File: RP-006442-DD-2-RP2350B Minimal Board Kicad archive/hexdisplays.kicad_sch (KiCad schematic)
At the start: 0 parts

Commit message: Created HT16K33-28SOP symbol
assigned new symbol footprint the pre-defined footprint for SOP-28 package
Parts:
- added U8: HT16K33A-28SOP, Package_SO:SOP-28_8.4x18.16mm_P1.27mm, symbol Driver_LED:HT16K33A-28SOP
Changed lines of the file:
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@@
 	(generator_version "9.0")
 	(paper "A4")
+	(symbol
+		(lib_id "Driver_LED:HT16K33A-28SOP")
+		(at 113.03 82.55 0)
+		(unit 1)
+		(exclude_from_sim no)
+		(in_bom yes)
+		(on_board yes)
+		(dnp no)
+		(fields_autoplaced yes)
+		(property "Reference" "U8"
+			(at 128.905 76.2 0)
+			(effects
+				(font
+					(size 1.27 1.27)
+				)
+			)
+		)
+		(property "Value" "HT16K33A-28SOP"
+			(at 128.905 78.74 0)
+			(effects
+				(font
+					(size 1.27 1.27)
+				)
+			)
+		)
+		(property "Footprint" "Package_SO:SOP-28_8.4x18.16mm_P1.27mm"
+			(at 129.032 121.412 0)
+			(effects
+				(font
+					(size 1.27 1.27)
+				)
+				(hide yes)
+			)
+		)
+		(property "Datasheet" "https://www.holtek.com/webapi/116711/HT16K33Av102.pdf"
+			(at 127.254 78.232 0)
+			(effects
+				(font
+					(size 1.27 1.27)
+				)
+				(hide yes)
+			)
+		)
+		(property "Description" "RAM Mapping 16×8 LED Controller Driver with Keyscan"
+			(at 127.254 75.946 0)
+			(effects
+				(font
+					(size 1.27 1.27)
+				)
+				(hide yes)
+			)
+		)
+		(pin "1"
+		)
+		(pin "7"
+		)
+		(pin "6"
+		)
+		(pin "5"
+		)
+		(pin "4"
+		)
+		(pin "8"
+		)
+		(pin "9"
+		)
+		(pin "19"
+		)
+		(pin "15"
+		)
+		(pin "20"
+		)
+		(pin "2"
+		)
+		(pin "23"
+		)
+		(pin "24"
+		)
+		(pin "25"
+		)
+		(pin "26"
+		)
+		(pin "28"
+		)
+		(pin "27"
+		)
+		(pin "14"
+		)
+		(pin "13"
+		)
+		(pin "12"
+		)
+		(pin "11"
+		)
+		(pin "10"
+		)
+		(pin "22"
+		)
+		(pin "21"
+		)
+		(pin "3"
+		)
+		(pin "16"
+		)
+		(pin "18"
+		)
+		(pin "17"
+		)
+		(instances
+			(project ""
+				(path "/94683f5c-9cd9-448e-be96-9792537b5cb8/09473c75-4602-45fc-a2db-44d591bf96bf"
+					(reference "U8")
+					(unit 1)
+				)
+			)
+		)
+	)
 )

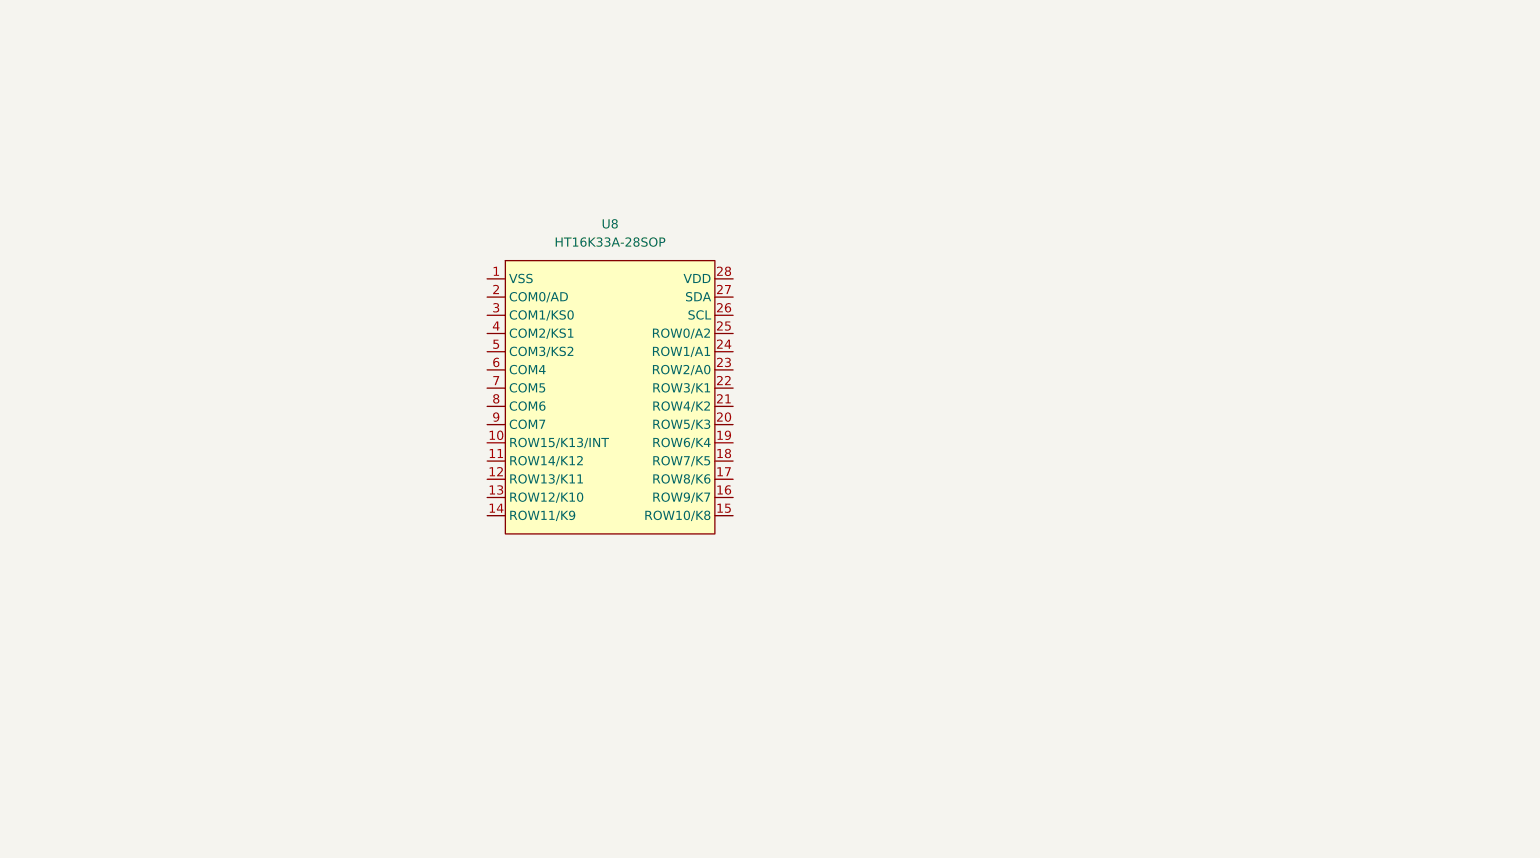
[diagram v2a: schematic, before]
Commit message: Update hex displays
Added 7-segment display symbol, labels, i2c pull-up resistors, capacitor.

Synced added components to pcb.
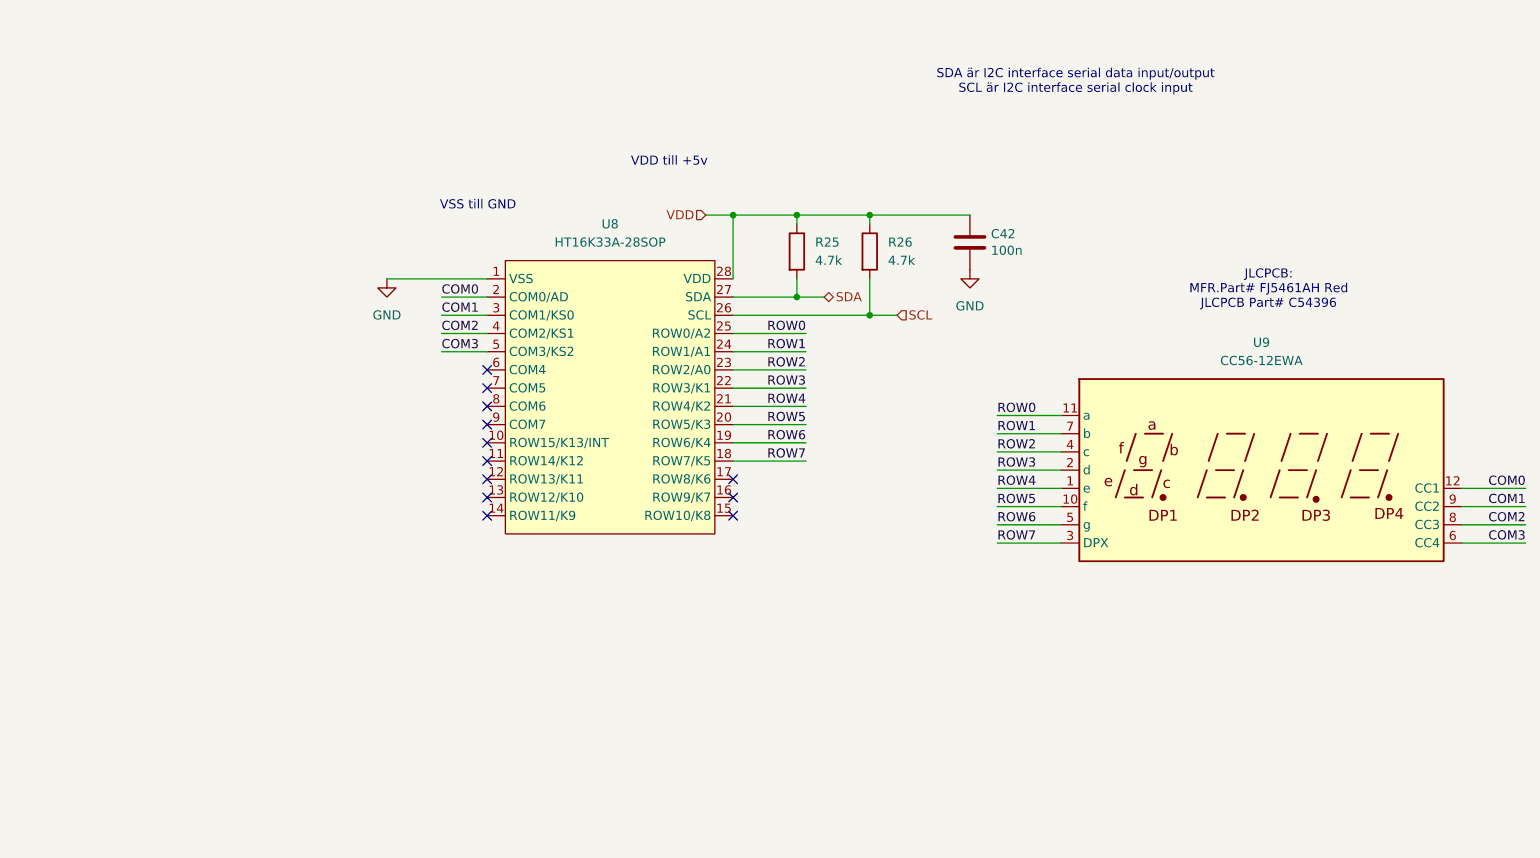
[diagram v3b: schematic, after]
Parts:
- added C42: 100n, Capacitor_SMD:C_0402_1005Metric, symbol Device:C
- added R25, R26: 4.7k, Resistor_SMD:R_0402_1005Metric, symbol Device:R
- added U9: CC56-12EWA, Display_7Segment:CA56-12EWA, symbol Display_Character:CC56-12EWA
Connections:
- net GND: now reaches U8.1 (VSS)
- net GND: now also C42.2
- net ROW7: now reaches U8.18 (ROW7/K5)
- net ROW7: now also U9.3 (DPX)
- net ROW6: now reaches U8.19 (ROW6/K4)
- net ROW6: now also U9.5 (g)
- net COM0: now reaches U8.2 (COM0/AD)
- net COM0: now also U9.12 (CC1)
- net ROW5: now reaches U8.20 (ROW5/K3)
- net ROW5: now also U9.10 (f)
- net ROW4: now reaches U8.21 (ROW4/K2)
- net ROW4: now also U9.1 (e)
- net ROW3: now reaches U8.22 (ROW3/K1)
- net ROW3: now also U9.2 (d)
- net ROW2: now reaches U8.23 (ROW2/A0)
- net ROW2: now also U9.4 (c)
- net ROW1: now reaches U8.24 (ROW1/A1)
- net ROW1: now also U9.7 (b)
- net ROW0: now reaches U8.25 (ROW0/A2)
- net ROW0: now also U9.11 (a)
- net SCL: now reaches U8.26 (SCL)
- net SCL: now also R26.2
- net SDA: now reaches U8.27 (SDA)
- net SDA: now also R25.2
- net VDD: now reaches U8.28 (VDD)
- net VDD: now also C42.1, R25.1, R26.1
- net COM1: now reaches U8.3 (COM1/KS0)
- net COM1: now also U9.9 (CC2)
- net COM2: now reaches U8.4 (COM2/KS1)
- net COM2: now also U9.8 (CC3)
- net COM3: now reaches U8.5 (COM3/KS2)
- net COM3: now also U9.6 (CC4)
- no-connect marks 0 -> 12
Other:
- note added: "JLCPCB: MFR.Part# FJ5461AH Red JLCPCB Part# C54396"
- note added: "SDA är I2C interface serial data input/output SCL är I2C interface serial clock input"
- note added: "VDD till +5v"
- note added: "VSS till GND"

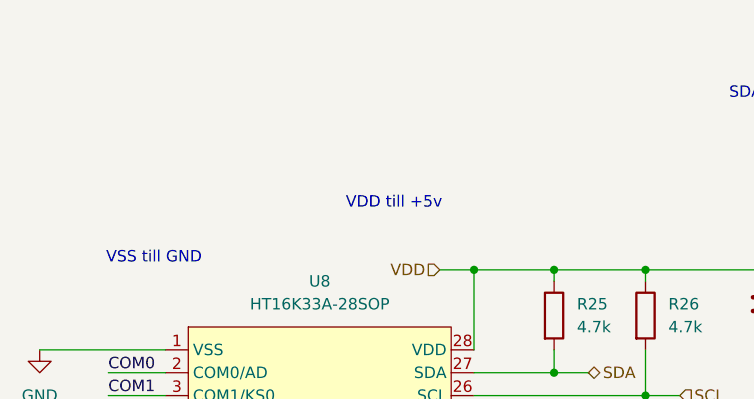
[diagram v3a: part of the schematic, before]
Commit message: Update hexdisplays.kicad_sch
added NCP1117-5.0 linear voltage regulator symbol
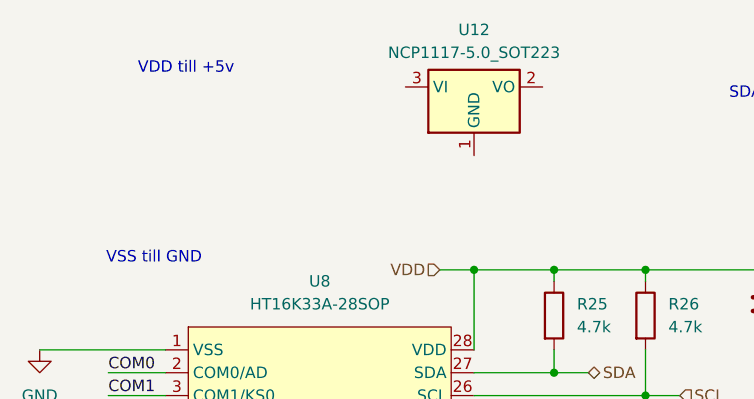
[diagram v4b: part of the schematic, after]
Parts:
- added U12: NCP1117-5.0_SOT223, Package_TO_SOT_SMD:SOT-223-3_TabPin2, symbol Regulator_Linear:NCP1117-5.0_SOT223
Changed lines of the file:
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@@
 	(text "VDD till +5v"
 		(exclude_from_sim no)
-		(at 137.16 67.564 0)
+		(at 114.046 52.578 0)
 		(effects
 			(font
@@
 					(unit 1)
 				)
+			)
+		)
+	)
+	(symbol
+		(lib_id "Regulator_Linear:NCP1117-5.0_SOT223")
+		(at 146.05 54.61 0)
+		(unit 1)
+		(exclude_from_sim no)
+		(in_bom yes)
+		(on_board yes)
+		(dnp no)
+		(fields_autoplaced yes)
+		(property "Reference" "U12"
+			(at 146.05 48.26 0)
+			(effects
+				(font
+					(size 1.27 1.27)
+				)
+			)
+		)
+		(property "Value" "NCP1117-5.0_SOT223"
+			(at 146.05 50.8 0)
+			(effects
+				(font
+					(size 1.27 1.27)
+				)
+			)
+		)
+		(property "Footprint" "Package_TO_SOT_SMD:SOT-223-3_TabPin2"
+			(at 146.05 49.53 0)
+			(effects
+				(font
+					(size 1.27 1.27)
+				)
+				(hide yes)
+			)
+		)
+		(property "Datasheet" "http://www.onsemi.com/pub_link/Collateral/NCP1117-D.PDF"
+			(at 148.59 60.96 0)
+			(effects
+				(font
+					(size 1.27 1.27)
+				)
+				(hide yes)
+			)
+		)
+		(property "Description" "1A Low drop-out regulator, Fixed Output 5V, SOT-223"
+			(at 146.05 54.61 0)
+			(effects
+				(font
+					(size 1.27 1.27)
+				)
+				(hide yes)
+			)
+		)
+		(pin "1"
+		)
+		(pin "2"
+		)
+		(pin "3"
+		)
+		(instances
+			(project ""
+				(path "/94683f5c-9cd9-448e-be96-9792537b5cb8/09473c75-4602-45fc-a2db-44d591bf96bf"
+					(reference "U12")
+					(unit 1)
+				)

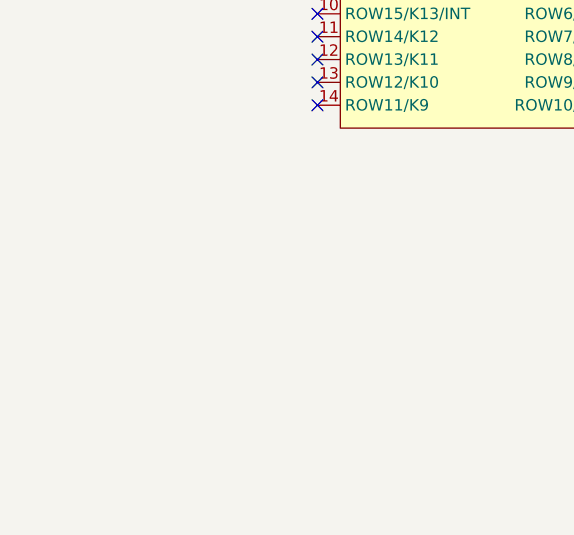
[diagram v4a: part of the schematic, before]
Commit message: Update hexdisplays.kicad_sch
Created symbol for a HT16K33A-24SSOP ic with existing SSOP-24 footprint
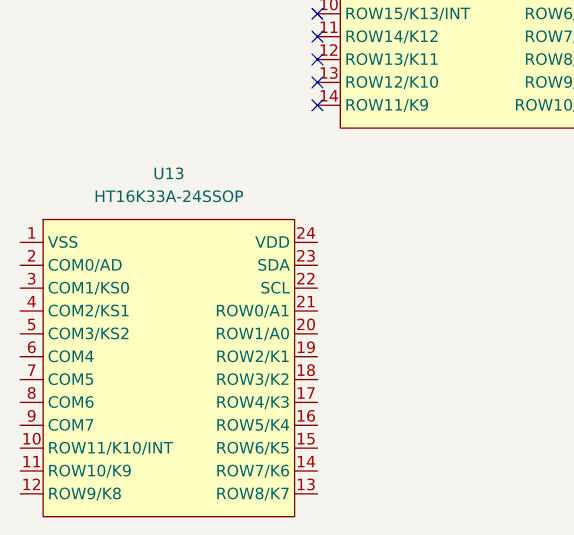
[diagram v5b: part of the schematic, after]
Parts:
- added U13: HT16K33A-24SSOP, Package_SO:SSOP-24_3.9x8.7mm_P0.635mm, symbol Driver_LED:HT16K33A-24SSOP
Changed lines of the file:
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@@
+	)
+	(symbol
+		(lib_id "Driver_LED:HT16K33A-24SSOP")
+		(at 81.28 129.54 0)
+		(unit 1)
+		(exclude_from_sim no)
+		(in_bom yes)
+		(on_board yes)
+		(dnp no)
+		(fields_autoplaced yes)
+		(property "Reference" "U13"
+			(at 95.25 124.46 0)
+			(effects
+				(font
+					(size 1.27 1.27)
+				)
+			)
+		)
+		(property "Value" "HT16K33A-24SSOP"
+			(at 95.25 127 0)
+			(effects
+				(font
+					(size 1.27 1.27)
+				)
+			)
+		)
+		(property "Footprint" "Package_SO:SSOP-24_3.9x8.7mm_P0.635mm"
+			(at 94.742 147.32 90)
+			(effects
+				(font
+					(size 1.27 1.27)
+				)
+				(hide yes)
+			)
+		)
+		(property "Datasheet" ""
+			(at 81.28 129.54 0)
+			(effects
+				(font
+					(size 1.27 1.27)
+				)
+				(hide yes)
+			)
+		)
+		(property "Description" ""
+			(at 81.28 129.54 0)
+			(effects
+				(font
+					(size 1.27 1.27)
+				)
+				(hide yes)
+			)
+		)
+		(pin "8"
+		)
+		(pin "17"
+		)
+		(pin "7"
+		)
+		(pin "24"
+		)
+		(pin "22"
+		)
+		(pin "6"
+		)
+		(pin "5"
+		)
+		(pin "4"
+		)
+		(pin "3"
+		)
+		(pin "9"
+		)
+		(pin "18"
+		)
+		(pin "1"
+		)
+		(pin "11"
+		)
+		(pin "20"
+		)
+		(pin "10"
+		)
+		(pin "2"
+		)
+		(pin "15"
+		)
+		(pin "21"
+		)
+		(pin "23"
+		)
+		(pin "13"
+		)
+		(pin "12"
+		)
+		(pin "19"
+		)
+		(pin "14"
+		)
+		(pin "16"
+		)
+		(instances
+			(project ""
+				(path "/94683f5c-9cd9-448e-be96-9792537b5cb8/09473c75-4602-45fc-a2db-44d591bf96bf"
+					(reference "U13")
+					(unit 1)
+				)
+			)
+		)
 	)
 	(symbol

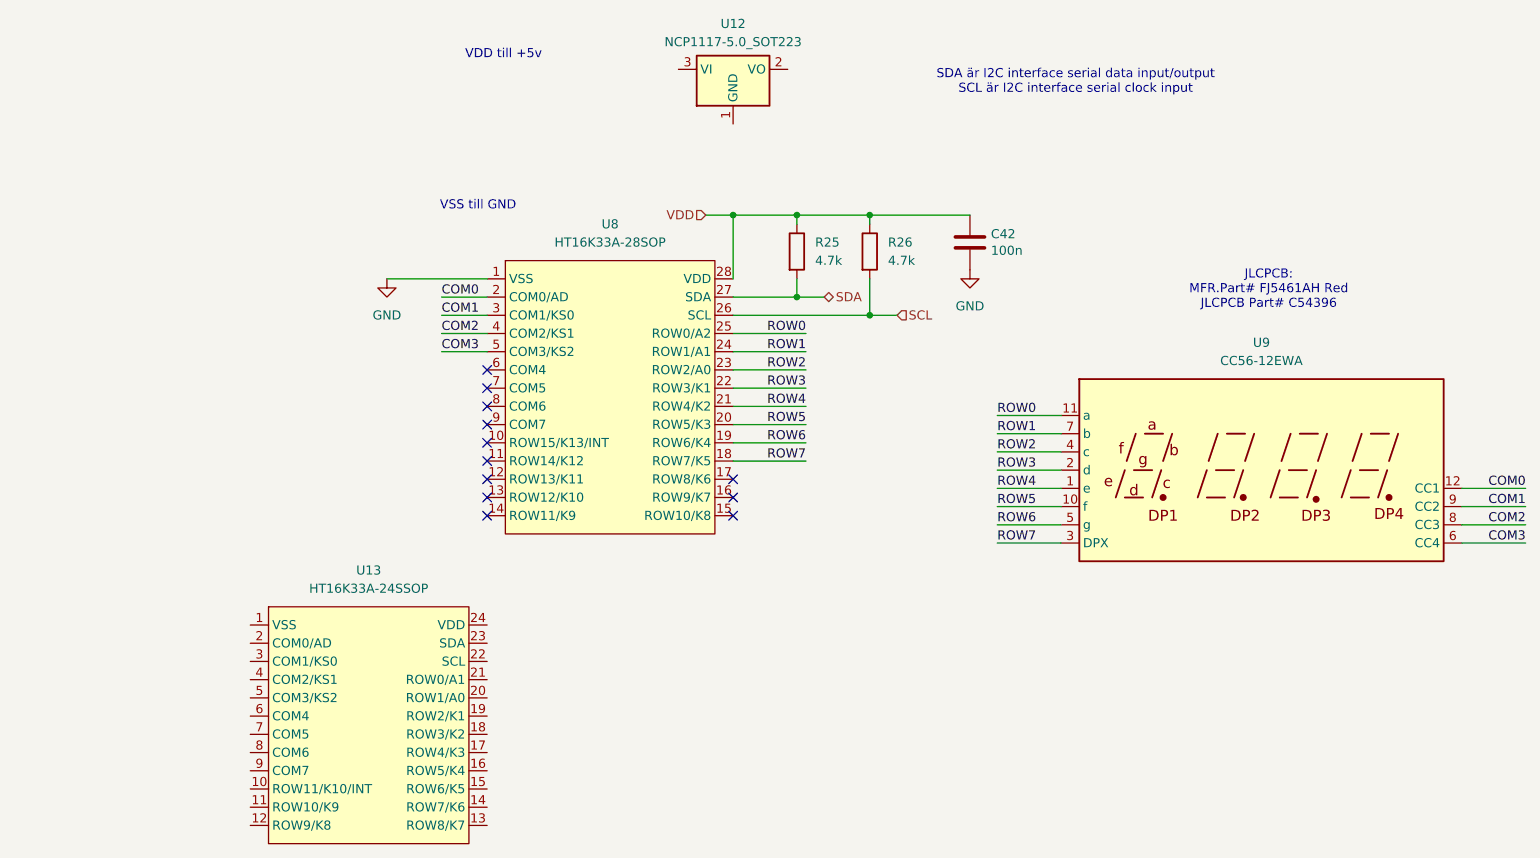
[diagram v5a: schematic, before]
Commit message: Update to schematic and pcb
Changed ht16k33 package from 28SOP to 24SSOP

Placed pcb footprints
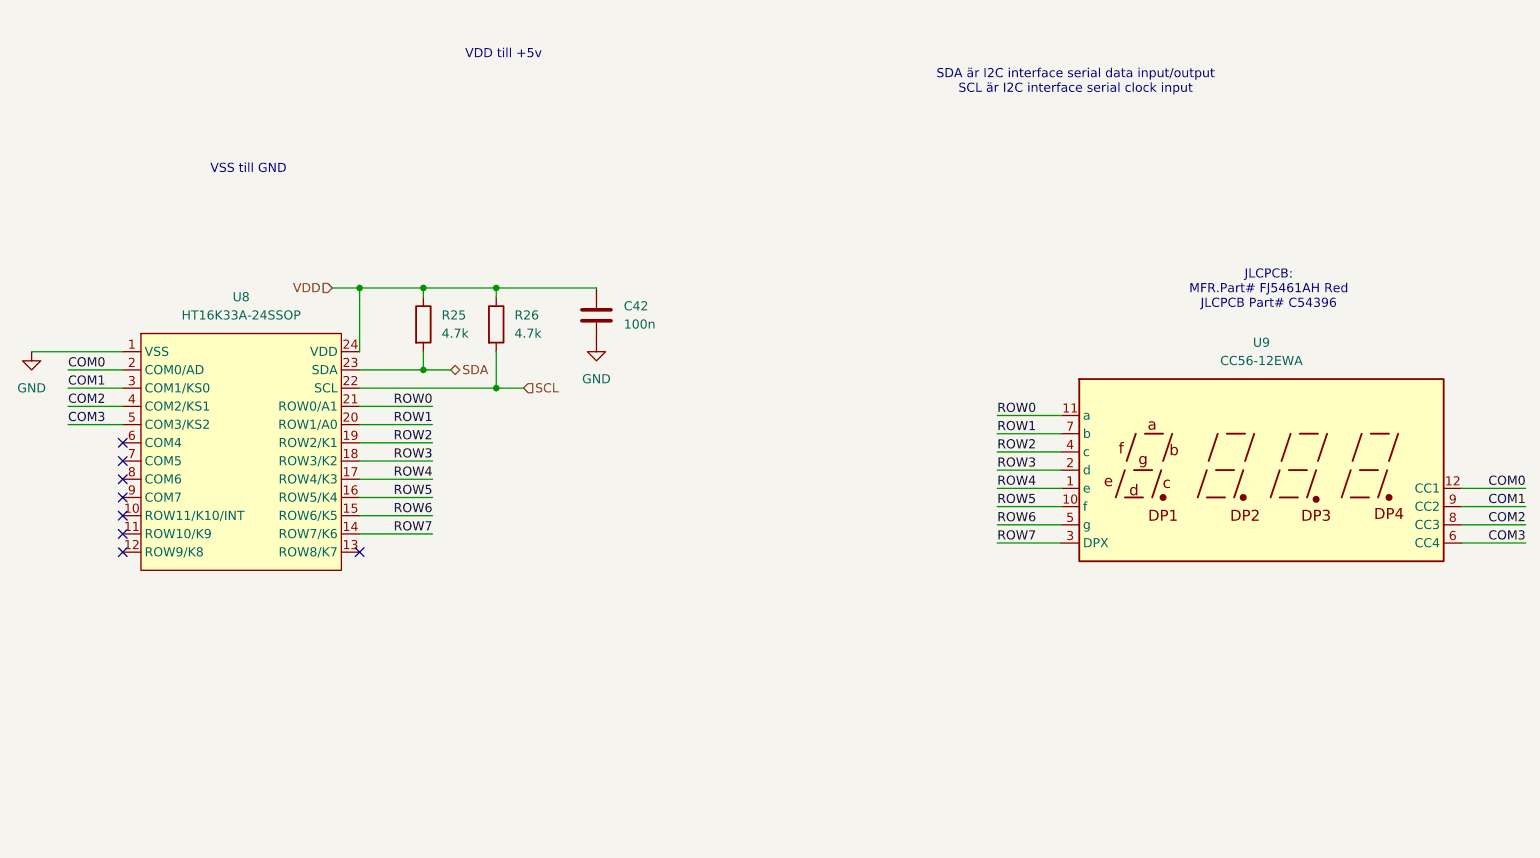
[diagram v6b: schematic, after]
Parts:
- removed U12: NCP1117-5.0_SOT223, Package_TO_SOT_SMD:SOT-223-3_TabPin2, symbol Regulator_Linear:NCP1117-5.0_SOT223
- removed U13: HT16K33A-24SSOP, Package_SO:SSOP-24_3.9x8.7mm_P0.635mm, symbol Driver_LED:HT16K33A-24SSOP
- removed U8: HT16K33A-28SOP, Package_SO:SOP-28_8.4x18.16mm_P1.27mm, symbol Driver_LED:HT16K33A-28SOP
- added U8: HT16K33A-24SSOP, Package_SO:SSOP-24_3.9x8.7mm_P0.635mm, symbol Driver_LED:HT16K33A-24SSOP
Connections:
- net COM0: now also U8.2 (COM0/AD)
- net COM1: now also U8.3 (COM1/KS0)
- net COM2: now also U8.4 (COM2/KS1)
- net COM3: now also U8.5 (COM3/KS2)
- net GND: now also U8.1 (VSS)
- net ROW0: now also U8.21 (ROW0/A1)
- net ROW1: now also U8.20 (ROW1/A0)
- net ROW2: now also U8.19 (ROW2/K1)
- net ROW3: now also U8.18 (ROW3/K2)
- net ROW4: now also U8.17 (ROW4/K3)
- net ROW5: now also U8.16 (ROW5/K4)
- net ROW6: now also U8.15 (ROW6/K5)
- net ROW7: now also U8.14 (ROW7/K6)
- net SCL: now also U8.22 (SCL)
- net SDA: now also U8.23 (SDA)
- net VDD: now also U8.24 (VDD)
- no-connect marks 12 -> 8

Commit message: Update
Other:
- note added: "Holtek Semicon HT16K33A-24SSOP SSOP-24 LED Drivers ROHS"
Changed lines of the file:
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@@
+		)
+	)
+	(text "Holtek Semicon\nHT16K33A-24SSOP\nSSOP-24 LED Drivers ROHS"
+		(exclude_from_sim no)
+		(at 78.74 128.27 0)
+		(effects
+			(font
+				(size 1.27 1.27)
+			)
 		)
 	)
@@
 			)
 		)
-		(property "Datasheet" ""
+		(property "Datasheet" "https://www.holtek.com/webapi/116711/HT16K33Av102.pdf"
 			(at 63.5 91.44 0)
 			(effects
